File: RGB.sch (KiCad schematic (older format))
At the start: 7 parts

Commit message: Major upgrade
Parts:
- D10, D11, D12, D13, D7, D8, D9: footprint LED_SMD:LED_WS2812B_PLCC4_5.0x5.0mm_P3.2mm -> WS2812-2020:WS28122020
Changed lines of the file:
@@
 F 0 "D7" H 3650 4050 50  0000 L CNN
 F 1 "WS2812B" H 3650 3950 50  0000 L CNN
-F 2 "LED_SMD:LED_WS2812B_PLCC4_5.0x5.0mm_P3.2mm" H 3650 3400 50  0001 L TNN
+F 2 "WS2812-2020:WS28122020" H 3650 3400 50  0001 L TNN
 F 3 "https://cdn-shop.adafruit.com/datasheets/WS2812B.pdf" H 3700 3325 50  0001 L TNN
 	1    3600 3700
@@
 F 0 "D8" H 4250 4050 50  0000 L CNN
 F 1 "WS2812B" H 4250 3950 50  0000 L CNN
-F 2 "LED_SMD:LED_WS2812B_PLCC4_5.0x5.0mm_P3.2mm" H 4250 3400 50  0001 L TNN
+F 2 "WS2812-2020:WS28122020" H 4250 3400 50  0001 L TNN
 F 3 "https://cdn-shop.adafruit.com/datasheets/WS2812B.pdf" H 4300 3325 50  0001 L TNN
 	1    4200 3700
@@
 F 0 "D9" H 4850 4050 50  0000 L CNN
 F 1 "WS2812B" H 4850 3950 50  0000 L CNN
-F 2 "LED_SMD:LED_WS2812B_PLCC4_5.0x5.0mm_P3.2mm" H 4850 3400 50  0001 L TNN
+F 2 "WS2812-2020:WS28122020" H 4850 3400 50  0001 L TNN
 F 3 "https://cdn-shop.adafruit.com/datasheets/WS2812B.pdf" H 4900 3325 50  0001 L TNN
 	1    4800 3700
@@
 F 0 "D10" H 5450 4050 50  0000 L CNN
 F 1 "WS2812B" H 5450 3950 50  0000 L CNN
-F 2 "LED_SMD:LED_WS2812B_PLCC4_5.0x5.0mm_P3.2mm" H 5450 3400 50  0001 L TNN
+F 2 "WS2812-2020:WS28122020" H 5450 3400 50  0001 L TNN
 F 3 "https://cdn-shop.adafruit.com/datasheets/WS2812B.pdf" H 5500 3325 50  0001 L TNN
 	1    5400 3700
@@
 F 0 "D11" H 6050 4050 50  0000 L CNN
 F 1 "WS2812B" H 6050 3950 50  0000 L CNN
-F 2 "LED_SMD:LED_WS2812B_PLCC4_5.0x5.0mm_P3.2mm" H 6050 3400 50  0001 L TNN
+F 2 "WS2812-2020:WS28122020" H 6050 3400 50  0001 L TNN
 F 3 "https://cdn-shop.adafruit.com/datasheets/WS2812B.pdf" H 6100 3325 50  0001 L TNN
 	1    6000 3700
@@
 F 0 "D12" H 6650 4050 50  0000 L CNN
 F 1 "WS2812B" H 6650 3950 50  0000 L CNN
-F 2 "LED_SMD:LED_WS2812B_PLCC4_5.0x5.0mm_P3.2mm" H 6650 3400 50  0001 L TNN
+F 2 "WS2812-2020:WS28122020" H 6650 3400 50  0001 L TNN
 F 3 "https://cdn-shop.adafruit.com/datasheets/WS2812B.pdf" H 6700 3325 50  0001 L TNN
 	1    6600 3700
@@
 F 0 "D13" H 7250 4050 50  0000 L CNN
 F 1 "WS2812B" H 7250 3950 50  0000 L CNN
-F 2 "LED_SMD:LED_WS2812B_PLCC4_5.0x5.0mm_P3.2mm" H 7250 3400 50  0001 L TNN
+F 2 "WS2812-2020:WS28122020" H 7250 3400 50  0001 L TNN
 F 3 "https://cdn-shop.adafruit.com/datasheets/WS2812B.pdf" H 7300 3325 50  0001 L TNN
 	1    7200 3700

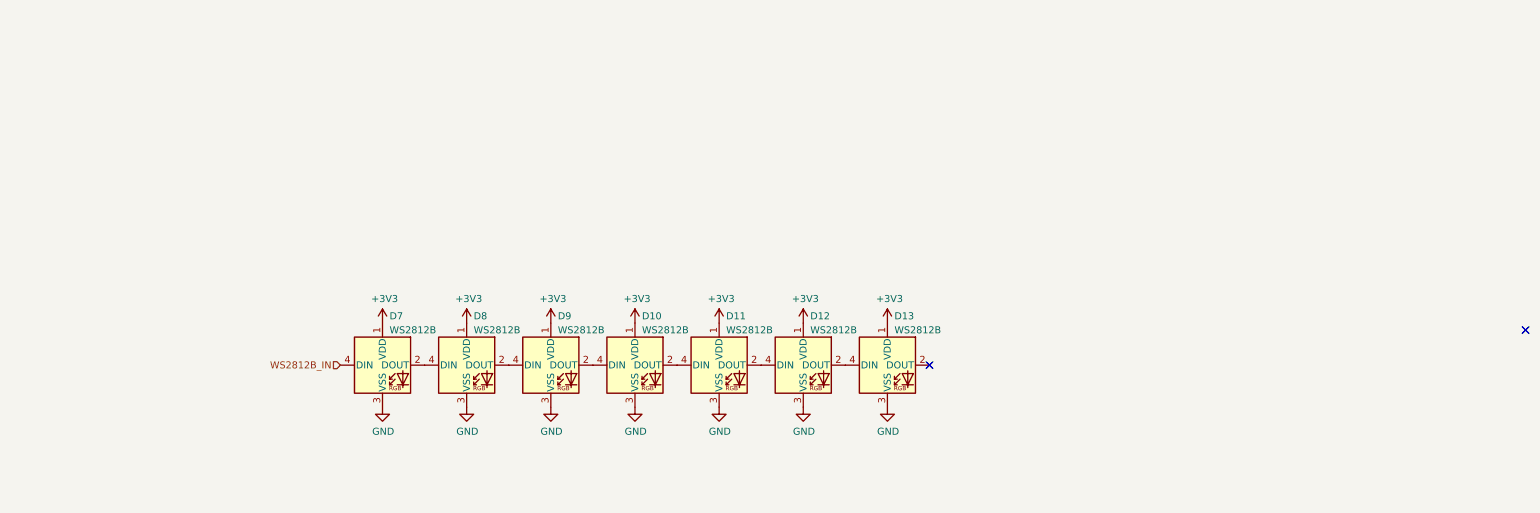
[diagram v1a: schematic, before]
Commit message: Added 2 RGB leds
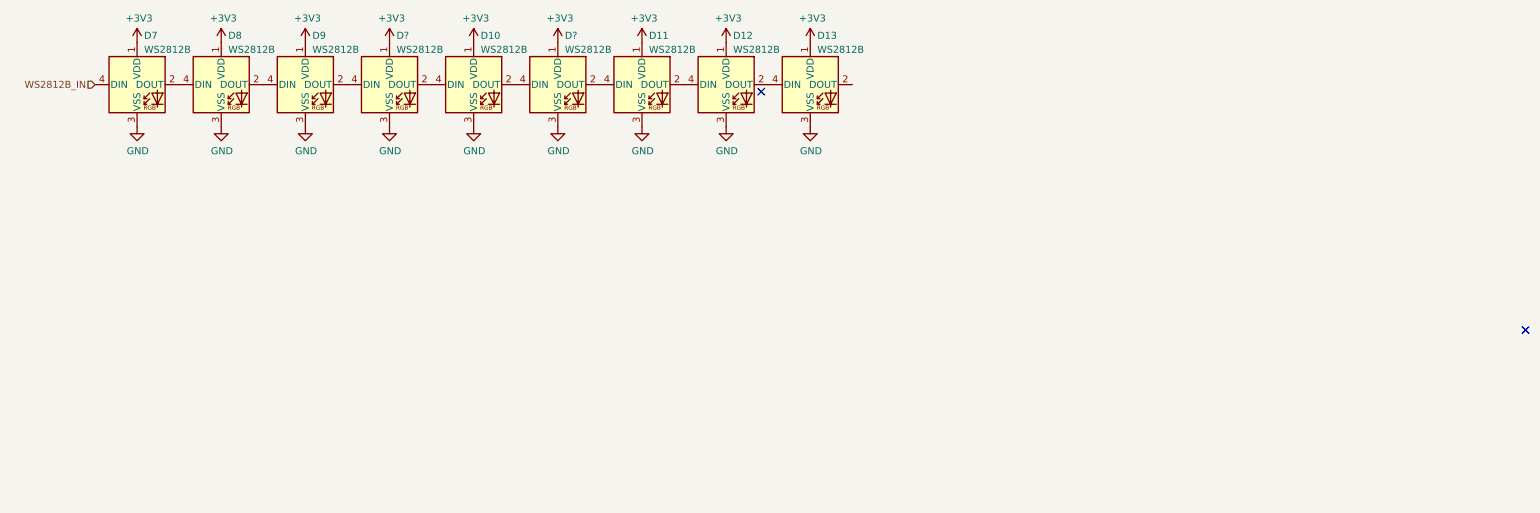
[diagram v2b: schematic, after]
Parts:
- added D? (x2): WS2812B, WS2812-2020:WS28122020, symbol LED:WS2812B
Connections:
- net +3V3: now also D?.1 (VDD), D?.1 (VDD)
- net GND: now also D?.3 (VSS), D?.3 (VSS)
- net at D10.4 (DIN): now also D?.2 (DOUT); no longer D9.2 (DOUT)
- net at D11.4 (DIN): now also D?.2 (DOUT); no longer D10.2 (DOUT)
- new net: D9.2 (DOUT), D?.4 (DIN)
- new net: D10.2 (DOUT), D?.4 (DIN)
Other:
- moved on the sheet: D10, D11, D12, D13, D7, D8, D9

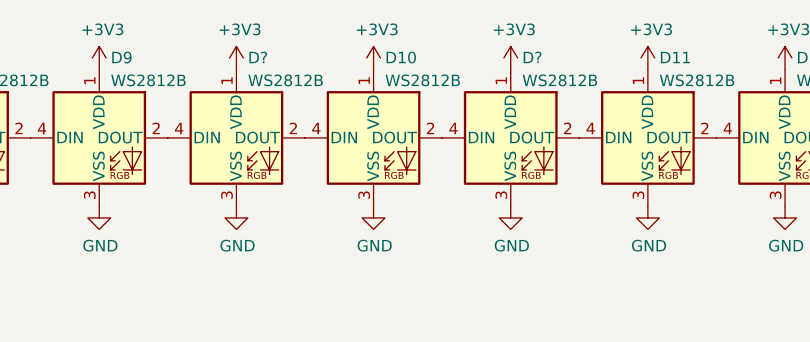
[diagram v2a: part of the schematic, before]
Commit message: PWR correction in RGB sch
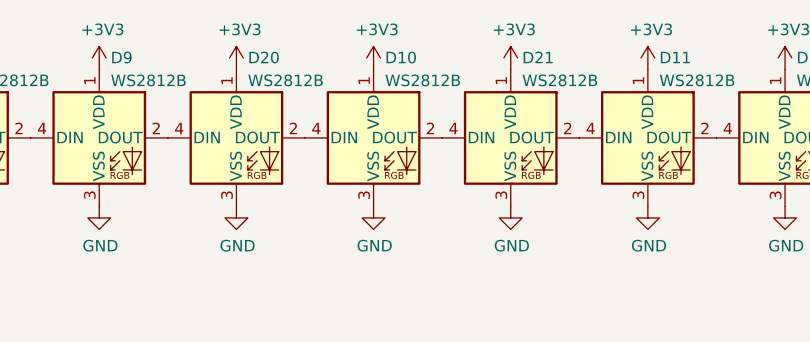
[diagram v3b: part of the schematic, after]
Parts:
- gave numbers to parts that had none: 2
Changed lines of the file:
@@
 $EndComp
 $Comp
-L power:GND #PWR?
+L power:GND #PWR0232
 U 1 1 5E69FEED
 P 3650 2000
-F 0 "#PWR?" H 3650 1750 50  0001 C CNN
+F 0 "#PWR0232" H 3650 1750 50  0001 C CNN
 F 1 "GND" H 3655 1827 50  0000 C CNN
 F 2 "" H 3650 2000 50  0001 C CNN
@@
 $EndComp
 $Comp
-L power:+3V3 #PWR?
+L power:+3V3 #PWR0233
 U 1 1 5E69FEF3
 P 3650 1400
-F 0 "#PWR?" H 3650 1250 50  0001 C CNN
+F 0 "#PWR0233" H 3650 1250 50  0001 C CNN
 F 1 "+3V3" H 3665 1573 50  0000 C CNN
 F 2 "" H 3650 1400 50  0001 C CNN
@@
 $EndComp
 $Comp
-L LED:WS2812B D?
+L LED:WS2812B D20
 U 1 1 5E69FEF9
 P 3650 1700
-F 0 "D?" H 3700 2050 50  0000 L CNN
+F 0 "D20" H 3700 2050 50  0000 L CNN
 F 1 "WS2812B" H 3700 1950 50  0000 L CNN
 F 2 "WS2812-2020:WS28122020" H 3700 1400 50  0001 L TNN
@@
 $EndComp
 $Comp
-L power:GND #PWR?
+L power:GND #PWR0234
 U 1 1 5E6A7A33
 P 4850 2000
-F 0 "#PWR?" H 4850 1750 50  0001 C CNN
+F 0 "#PWR0234" H 4850 1750 50  0001 C CNN
 F 1 "GND" H 4855 1827 50  0000 C CNN
 F 2 "" H 4850 2000 50  0001 C CNN
@@
 $EndComp
 $Comp
-L power:+3V3 #PWR?
+L power:+3V3 #PWR0235
 U 1 1 5E6A7A39
 P 4850 1400
-F 0 "#PWR?" H 4850 1250 50  0001 C CNN
+F 0 "#PWR0235" H 4850 1250 50  0001 C CNN
 F 1 "+3V3" H 4865 1573 50  0000 C CNN
 F 2 "" H 4850 1400 50  0001 C CNN
@@
 $EndComp
 $Comp
-L LED:WS2812B D?
+L LED:WS2812B D21
 U 1 1 5E6A7A3F
 P 4850 1700
-F 0 "D?" H 4900 2050 50  0000 L CNN
+F 0 "D21" H 4900 2050 50  0000 L CNN
 F 1 "WS2812B" H 4900 1950 50  0000 L CNN
 F 2 "WS2812-2020:WS28122020" H 4900 1400 50  0001 L TNN

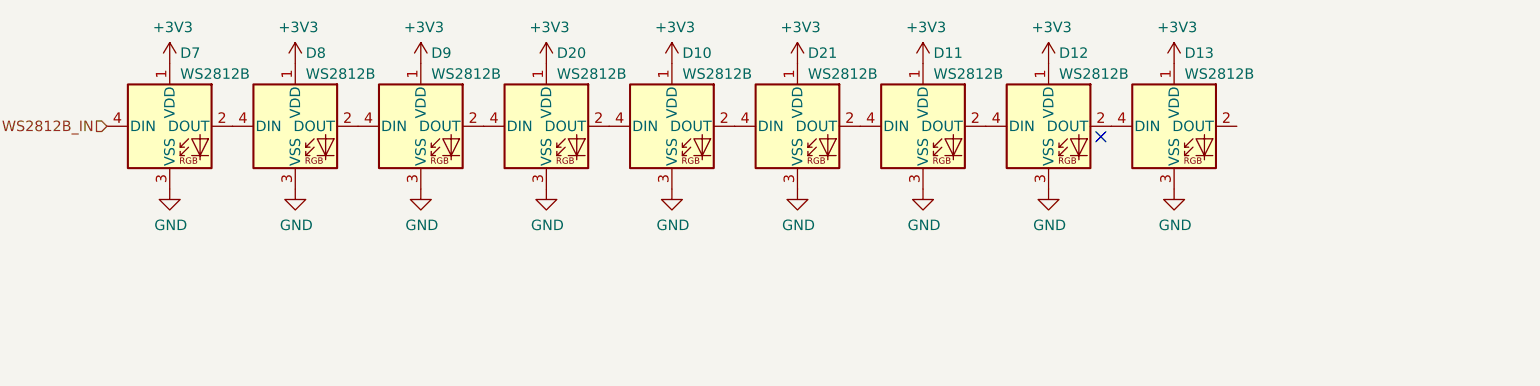
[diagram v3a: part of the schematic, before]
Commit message: Added 2 more RGB leds
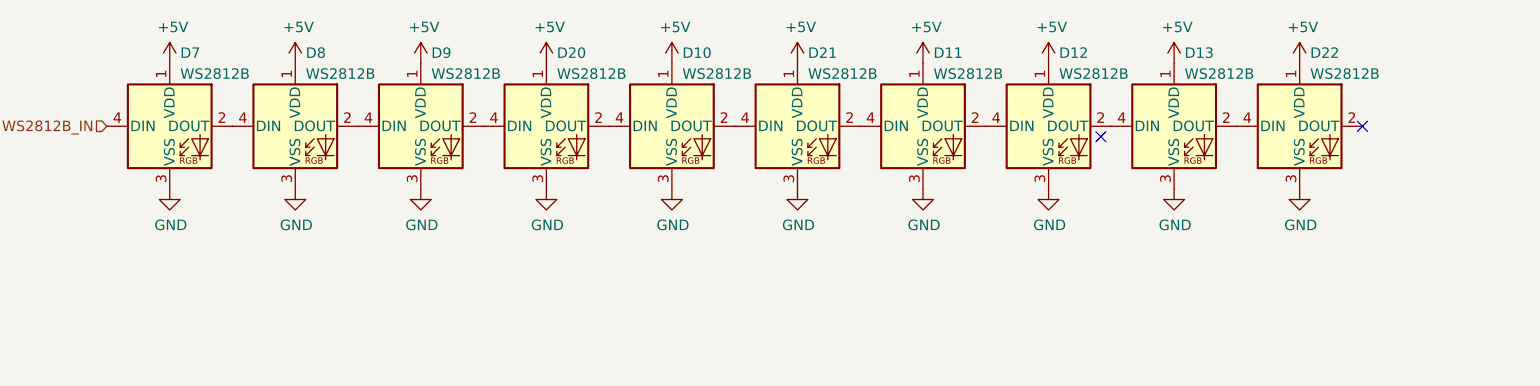
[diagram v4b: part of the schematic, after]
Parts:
- added D22: WS2812B, WS2812-2020:WS28122020, symbol LED:WS2812B
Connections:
- net GND: now also D22.3 (VSS)
- net at D13.2 (DOUT): now also D22.4 (DIN)
- net +3V3 renamed +5V
- net +5V: now also D22.1 (VDD)
- no-connect marks 2 -> 3
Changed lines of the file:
@@
-$EndComp
-$Comp
-L power:+3V3 #PWR0181
-U 1 1 5E81294E
-P 1850 1400
-F 0 "#PWR0181" H 1850 1250 50  0001 C CNN
-F 1 "+3V3" H 1865 1573 50  0000 C CNN
-F 2 "" H 1850 1400 50  0001 C CNN
-F 3 "" H 1850 1400 50  0001 C CNN
-	1    1850 1400
-	1    0    0    -1
 $EndComp
 $Comp
@@
 $EndComp
 $Comp
-L power:+3V3 #PWR0183
-U 1 1 5E8168B3
-P 2450 1400
-F 0 "#PWR0183" H 2450 1250 50  0001 C CNN
-F 1 "+3V3" H 2465 1573 50  0000 C CNN
-F 2 "" H 2450 1400 50  0001 C CNN
-F 3 "" H 2450 1400 50  0001 C CNN
-	1    2450 1400
-	1    0    0    -1
-$EndComp
-$Comp
 L power:GND #PWR0184
 U 1 1 5E8168B9
@@
 $EndComp
 $Comp
-L power:+3V3 #PWR0193
-U 1 1 5E819612
-P 6650 1400
-F 0 "#PWR0193" H 6650 1250 50  0001 C CNN
-F 1 "+3V3" H 6665 1573 50  0000 C CNN
-F 2 "" H 6650 1400 50  0001 C CNN
-F 3 "" H 6650 1400 50  0001 C CNN
-	1    6650 1400
-	1    0    0    -1
-$EndComp
-$Comp
 L LED:WS2812B D13
 U 1 1 5E81960C
@@
 $EndComp
 $Comp
-L power:+3V3 #PWR0191
-U 1 1 5E818C85
-P 6050 1400
-F 0 "#PWR0191" H 6050 1250 50  0001 C CNN
-F 1 "+3V3" H 6065 1573 50  0000 C CNN
-F 2 "" H 6050 1400 50  0001 C CNN
-F 3 "" H 6050 1400 50  0001 C CNN
-	1    6050 1400
-	1    0    0    -1
-$EndComp
-$Comp
 L LED:WS2812B D12
 U 1 1 5E818C7F
@@
 $EndComp
 $Comp
-L power:+3V3 #PWR0189
-U 1 1 5E818386
-P 5450 1400
-F 0 "#PWR0189" H 5450 1250 50  0001 C CNN
-F 1 "+3V3" H 5465 1573 50  0000 C CNN
-F 2 "" H 5450 1400 50  0001 C CNN
-F 3 "" H 5450 1400 50  0001 C CNN
-	1    5450 1400
-	1    0    0    -1
-$EndComp
-$Comp
 L LED:WS2812B D11
 U 1 1 5E818380
@@
 $EndComp
 $Comp
-L power:+3V3 #PWR0187
-U 1 1 5E8179E9
-P 4250 1400
-F 0 "#PWR0187" H 4250 1250 50  0001 C CNN
-F 1 "+3V3" H 4265 1573 50  0000 C CNN
-F 2 "" H 4250 1400 50  0001 C CNN
-F 3 "" H 4250 1400 50  0001 C CNN
-	1    4250 1400
-	1    0    0    -1
-$EndComp
-$Comp
 L LED:WS2812B D10
 U 1 1 5E8179E3
@@
 $EndComp
 $Comp
-L power:+3V3 #PWR0185
-U 1 1 5E817170
-P 3050 1400
-F 0 "#PWR0185" H 3050 1250 50  0001 C CNN
-F 1 "+3V3" H 3065 1573 50  0000 C CNN
-F 2 "" H 3050 1400 50  0001 C CNN
-F 3 "" H 3050 1400 50  0001 C CNN
-	1    3050 1400
-	1    0    0    -1
-$EndComp
-$Comp
 L LED:WS2812B D9
 U 1 1 5E81716A
@@
 $EndComp
 $Comp
-L power:+3V3 #PWR0233
-U 1 1 5E69FEF3
-P 3650 1400
-F 0 "#PWR0233" H 3650 1250 50  0001 C CNN
-F 1 "+3V3" H 3665 1573 50  0000 C CNN
-F 2 "" H 3650 1400 50  0001 C CNN
-F 3 "" H 3650 1400 50  0001 C CNN
-	1    3650 1400
-	1    0    0    -1
-$EndComp
-$Comp
 L LED:WS2812B D20
 U 1 1 5E69FEF9
@@
 $EndComp
 $Comp
-L power:+3V3 #PWR0235
-U 1 1 5E6A7A39
-P 4850 1400
-F 0 "#PWR0235" H 4850 1250 50  0001 C CNN
-F 1 "+3V3" H 4865 1573 50  0000 C CNN
-F 2 "" H 4850 1400 50  0001 C CNN
-F 3 "" H 4850 1400 50  0001 C CNN
-	1    4850 1400
-	1    0    0    -1
-$EndComp
-$Comp
 L LED:WS2812B D21
 U 1 1 5E6A7A3F
@@
 	1    0    0    -1
 $EndComp
+$Comp
+L power:GND #PWR0158
+U 1 1 5E702A72
+P 7250 2000
+F 0 "#PWR0158" H 7250 1750 50  0001 C CNN
+F 1 "GND" H 7255 1827 50  0000 C CNN
+F 2 "" H 7250 2000 50  0001 C CNN
+F 3 "" H 7250 2000 50  0001 C CNN
+	1    7250 2000
+	1    0    0    -1
+$EndComp
+$Comp
+L LED:WS2812B D22
+U 1 1 5E702A7E
+P 7250 1700
+F 0 "D22" H 7300 2050 50  0000 L CNN
+F 1 "WS2812B" H 7300 1950 50  0000 L CNN
+F 2 "WS2812-2020:WS28122020" H 7300 1400 50  0001 L TNN
+F 3 "https://cdn-shop.adafruit.com/datasheets/WS2812B.pdf" H 7350 1325 50  0001 L TNN
+	1    7250 1700
+	1    0    0    -1
+$EndComp
+NoConn ~ 7550 1700
+$Comp
+L power:+5V #PWR0163
+U 1 1 5E72F2B3
+P 1850 1400
+F 0 "#PWR0163" H 1850 1250 50  0001 C CNN
+F 1 "+5V" H 1865 1573 50  0000 C CNN
+F 2 "" H 1850 1400 50  0001 C CNN
+F 3 "" H 1850 1400 50  0001 C CNN
+	1    1850 1400
+	1    0    0    -1
+$EndComp
+$Comp
+L power:+5V #PWR0164
+U 1 1 5E72FAF9
+P 2450 1400
+F 0 "#PWR0164" H 2450 1250 50  0001 C CNN
+F 1 "+5V" H 2465 1573 50  0000 C CNN
+F 2 "" H 2450 1400 50  0001 C CNN
+F 3 "" H 2450 1400 50  0001 C CNN
+	1    2450 1400
+	1    0    0    -1
+$EndComp
+$Comp
+L power:+5V #PWR0165
+U 1 1 5E72FDD5
+P 3050 1400
+F 0 "#PWR0165" H 3050 1250 50  0001 C CNN
+F 1 "+5V" H 3065 1573 50  0000 C CNN
+F 2 "" H 3050 1400 50  0001 C CNN
+F 3 "" H 3050 1400 50  0001 C CNN
+	1    3050 1400
+	1    0    0    -1
+$EndComp
+$Comp
+L power:+5V #PWR0166
+U 1 1 5E7300B4
+P 3650 1400
+F 0 "#PWR0166" H 3650 1250 50  0001 C CNN
+F 1 "+5V" H 3665 1573 50  0000 C CNN
+F 2 "" H 3650 1400 50  0001 C CNN
+F 3 "" H 3650 1400 50  0001 C CNN
+	1    3650 1400
+	1    0    0    -1
+$EndComp
+$Comp
+L power:+5V #PWR0167
+U 1 1 5E7321A0
+P 4250 1400
+F 0 "#PWR0167" H 4250 1250 50  0001 C CNN
+F 1 "+5V" H 4265 1573 50  0000 C CNN
+F 2 "" H 4250 1400 50  0001 C CNN
+F 3 "" H 4250 1400 50  0001 C CNN
+	1    4250 1400
+	1    0    0    -1
+$EndComp
+$Comp
+L power:+5V #PWR0168
+U 1 1 5E732508
+P 4850 1400
+F 0 "#PWR0168" H 4850 1250 50  0001 C CNN
+F 1 "+5V" H 4865 1573 50  0000 C CNN
+F 2 "" H 4850 1400 50  0001 C CNN
+F 3 "" H 4850 1400 50  0001 C CNN
+	1    4850 1400
+	1    0    0    -1
+$EndComp
+$Comp
+L power:+5V #PWR0169
+U 1 1 5E732962
+P 5450 1400
+F 0 "#PWR0169" H 5450 1250 50  0001 C CNN
+F 1 "+5V" H 5465 1573 50  0000 C CNN
+F 2 "" H 5450 1400 50  0001 C CNN
+F 3 "" H 5450 1400 50  0001 C CNN
+	1    5450 1400
+	1    0    0    -1
+$EndComp
+$Comp
+L power:+5V #PWR0181
+U 1 1 5E732D7B
+P 6050 1400
+F 0 "#PWR0181" H 6050 1250 50  0001 C CNN
+F 1 "+5V" H 6065 1573 50  0000 C CNN
+F 2 "" H 6050 1400 50  0001 C CNN
+F 3 "" H 6050 1400 50  0001 C CNN
+	1    6050 1400
+	1    0    0    -1
+$EndComp
+$Comp
+L power:+5V #PWR0183
+U 1 1 5E73320D
+P 6650 1400
+F 0 "#PWR0183" H 6650 1250 50  0001 C CNN
+F 1 "+5V" H 6665 1573 50  0000 C CNN
+F 2 "" H 6650 1400 50  0001 C CNN
+F 3 "" H 6650 1400 50  0001 C CNN
+	1    6650 1400
+	1    0    0    -1
+$EndComp
+$Comp
+L power:+5V #PWR0185
+U 1 1 5E73360F
+P 7250 1400
+F 0 "#PWR0185" H 7250 1250 50  0001 C CNN
+F 1 "+5V" H 7265 1573 50  0000 C CNN
+F 2 "" H 7250 1400 50  0001 C CNN
+F 3 "" H 7250 1400 50  0001 C CNN
+	1    7250 1400
+	1    0    0    -1
+$EndComp

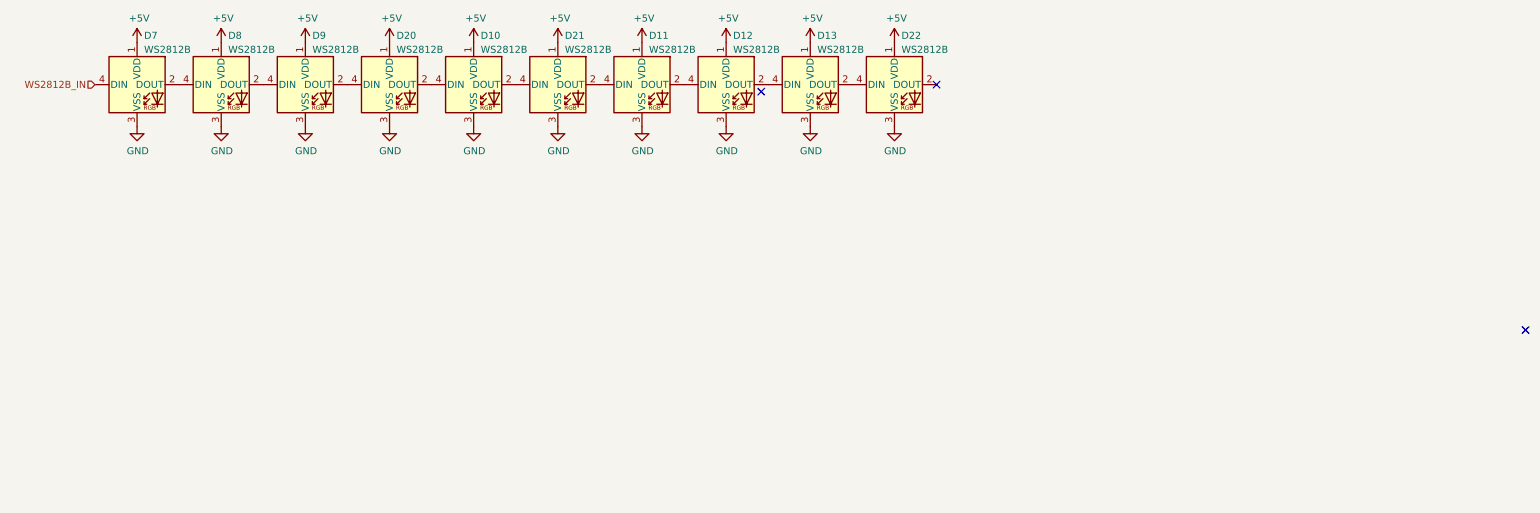
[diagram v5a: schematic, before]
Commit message: Changes in graphics, tweaks in power input, resistor values
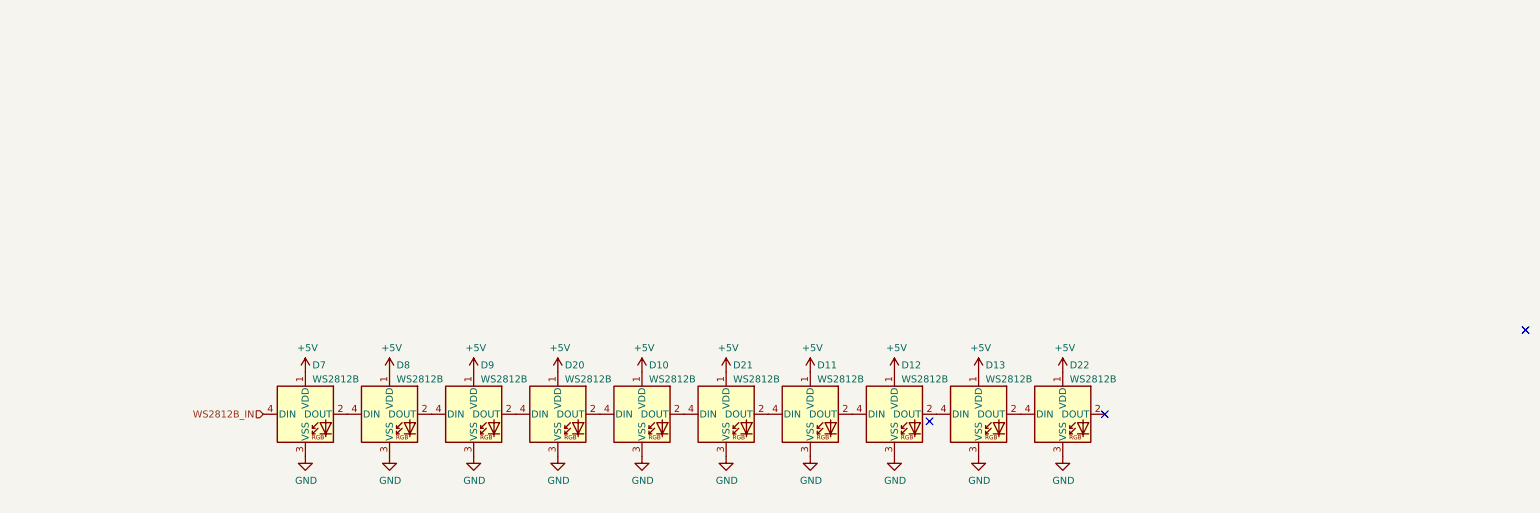
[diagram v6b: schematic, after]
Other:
- moved on the sheet: D10, D11, D12, D13, D20, D21, D22, D7, D8, D9
